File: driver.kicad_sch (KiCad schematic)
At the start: 39 parts, among them Q4 SIZ322DT, Q5 SIZ322DT, Q6 SIZ322DT, U4 TMC6200

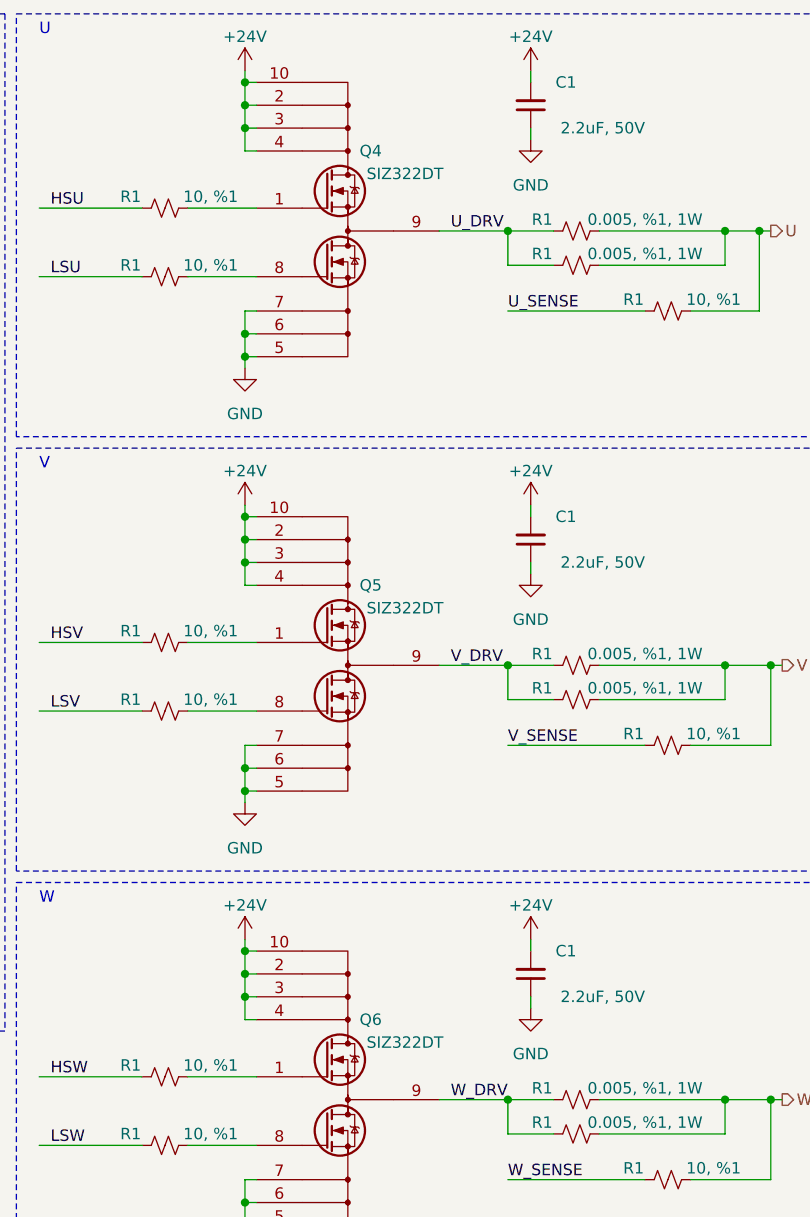
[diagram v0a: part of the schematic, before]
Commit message: Change the mosfets to SIZ342ADT.
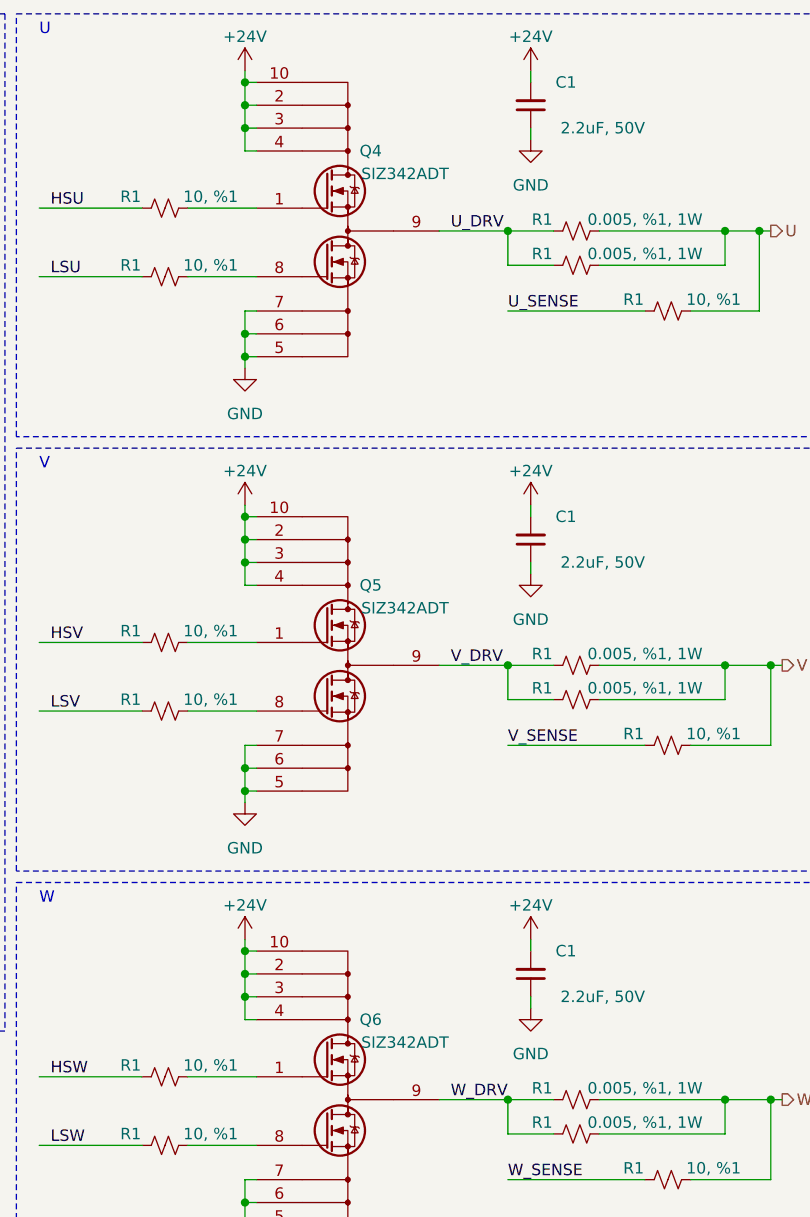
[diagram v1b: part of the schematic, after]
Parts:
- Q4, Q5, Q6: value SIZ322DT -> SIZ342ADT; MPN SIZ322DT-T1-GE3 -> SIZ342ADT-T1-GE3
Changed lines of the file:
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@@
       (effects (font (size 1.27 1.27)))
     )
-    (property "Value" "SIZ322DT" (at 226.06 129.54 0)
+    (property "Value" "SIZ342ADT" (at 226.06 129.54 0)
       (effects (font (size 1.27 1.27)))
     )
@@
       (effects (font (size 1.27 1.27)) (justify left top) hide)
     )
-    (property "MPN" "SIZ322DT-T1-GE3" (at 219.71 134.62 0)
+    (property "MPN" "SIZ342ADT-T1-GE3" (at 219.71 134.62 0)
       (effects (font (size 1.27 1.27)) hide)
     )
@@
       (effects (font (size 1.27 1.27)))
     )
-    (property "Value" "SIZ322DT" (at 226.06 33.02 0)
+    (property "Value" "SIZ342ADT" (at 226.06 33.02 0)
       (effects (font (size 1.27 1.27)))
     )
@@
       (effects (font (size 1.27 1.27)) (justify left top) hide)
     )
-    (property "MPN" "SIZ322DT-T1-GE3" (at 219.71 38.1 0)
+    (property "MPN" "SIZ342ADT-T1-GE3" (at 219.71 38.1 0)
       (effects (font (size 1.27 1.27)) hide)
     )
@@
       (effects (font (size 1.27 1.27)))
     )
-    (property "Value" "SIZ322DT" (at 226.06 81.28 0)
+    (property "Value" "SIZ342ADT" (at 226.06 81.28 0)
       (effects (font (size 1.27 1.27)))
     )
@@
       (effects (font (size 1.27 1.27)) (justify left top) hide)
     )
-    (property "MPN" "SIZ322DT-T1-GE3" (at 219.71 86.36 0)
-      (effects (font (size 1.27 1.27)) hide)
-    )
+    (property "MPN" "SIZ342ADT-T1-GE3" (at 219.71 86.36 0)
+      (effects (font (size 1.27 1.27)) hide)
+    )

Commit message: Small improvements.
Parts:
- C1: footprint Capacitor_SMD:C_1206_3216Metric -> Capacitor_SMD:C_0805_2012Metric; MPN CL31B225KBHNNNE -> CC0805KKX7R9BB225
- C22: value 100nF, 100V -> 100nF, 50V; footprint Capacitor_SMD:C_0603_1608Metric -> Capacitor_SMD:C_0402_1005Metric; MPN CL10B104KC8NNNC -> GRM155R71H104KE14J
- C22: MPN UMK212BB7225KG-T -> CC0805KKX7R9BB225
- C22: MPN CL05B104KB54PNC -> GRM155R71H104KE14J
- C22: value 22nF, 100V -> 22nF, 50V; footprint Capacitor_SMD:C_0603_1608Metric -> Capacitor_SMD:C_0402_1005Metric; MPN C0603C223K1RAC7867 -> GRM155R71H223KA12J
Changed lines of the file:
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@@
       (effects (font (size 1.27 1.27)) (justify left))
     )
-    (property "Value" "100nF, 100V" (at 59.69 41.91 0)
-      (effects (font (size 1.27 1.27)) (justify left))
-    )
-    (property "Footprint" "Capacitor_SMD:C_0603_1608Metric" (at 60.96 39.37 0)
+    (property "Value" "100nF, 50V" (at 59.69 41.91 0)
+      (effects (font (size 1.27 1.27)) (justify left))
+    )
+    (property "Footprint" "Capacitor_SMD:C_0402_1005Metric" (at 60.96 39.37 0)
       (effects (font (size 1.27 1.27)) hide)
     )
@@
       (effects (font (size 1.27 1.27)) hide)
     )
-    (property "MPN" "CL10B104KC8NNNC" (at 60.96 39.37 0)
+    (property "MPN" "GRM155R71H104KE14J" (at 60.96 39.37 0)
       (effects (font (size 1.27 1.27)) hide)
     )
@@
       (effects (font (size 1.27 1.27)) hide)
     )
-    (property "MPN" "UMK212BB7225KG-T" (at 33.02 55.88 0)
+    (property "MPN" "CC0805KKX7R9BB225" (at 33.02 55.88 0)
       (effects (font (size 1.27 1.27)) hide)
     )
@@
       (effects (font (size 1.27 1.27)) hide)
     )
-    (property "MPN" "CL05B104KB54PNC" (at 67.31 113.03 0)
+    (property "MPN" "GRM155R71H104KE14J" (at 67.31 113.03 0)
       (effects (font (size 1.27 1.27)) hide)
     )
@@
       (effects (font (size 1.27 1.27)) (justify left))
     )
-    (property "Value" "100nF, 100V" (at 111.76 30.48 90)
-      (effects (font (size 1.27 1.27)) (justify left))
-    )
-    (property "Footprint" "Capacitor_SMD:C_0603_1608Metric" (at 106.68 27.94 0)
+    (property "Value" "100nF, 50V" (at 111.76 30.48 90)
+      (effects (font (size 1.27 1.27)) (justify left))
+    )
+    (property "Footprint" "Capacitor_SMD:C_0402_1005Metric" (at 106.68 27.94 0)
       (effects (font (size 1.27 1.27)) hide)
     )
@@
       (effects (font (size 1.27 1.27)) hide)
     )
-    (property "MPN" "CL10B104KC8NNNC" (at 106.68 27.94 0)
+    (property "MPN" "GRM155R71H104KE14J" (at 106.68 27.94 0)
       (effects (font (size 1.27 1.27)) hide)
     )
@@
       (effects (font (size 1.27 1.27)) hide)
     )
-    (property "MPN" "CL05B104KB54PNC" (at 166.37 109.22 0)
+    (property "MPN" "GRM155R71H104KE14J" (at 166.37 109.22 0)
       (effects (font (size 1.27 1.27)) hide)
     )
@@
       (effects (font (size 1.27 1.27)) (justify left))
     )
-    (property "Value" "100nF, 100V" (at 130.81 33.02 0)
-      (effects (font (size 1.27 1.27)) (justify left))
-    )
-    (property "Footprint" "Capacitor_SMD:C_0603_1608Metric" (at 118.11 30.48 0)
+    (property "Value" "100nF, 50V" (at 130.81 33.02 0)
+      (effects (font (size 1.27 1.27)) (justify left))
+    )
+    (property "Footprint" "Capacitor_SMD:C_0402_1005Metric" (at 118.11 30.48 0)
       (effects (font (size 1.27 1.27)) hide)
     )
@@
       (effects (font (size 1.27 1.27)) hide)
     )
-    (property "MPN" "CL10B104KC8NNNC" (at 118.11 30.48 0)
+    (property "MPN" "GRM155R71H104KE14J" (at 118.11 30.48 0)
       (effects (font (size 1.27 1.27)) hide)
     )
@@
       (effects (font (size 1.27 1.27)) (justify left))
     )
-    (property "Value" "22nF, 100V" (at 97.79 30.48 90)
-      (effects (font (size 1.27 1.27)) (justify left))
-    )
-    (property "Footprint" "Capacitor_SMD:C_0603_1608Metric" (at 92.71 27.94 0)
+    (property "Value" "22nF, 50V" (at 97.79 30.48 90)
+      (effects (font (size 1.27 1.27)) (justify left))
+    )
+    (property "Footprint" "Capacitor_SMD:C_0402_1005Metric" (at 92.71 27.94 0)
       (effects (font (size 1.27 1.27)) hide)
     )
@@
       (effects (font (size 1.27 1.27)) hide)
     )
-    (property "MPN" "C0603C223K1RAC7867" (at 92.71 27.94 90)
+    (property "MPN" "GRM155R71H223KA12J" (at 92.71 27.94 90)
       (effects (font (size 1.27 1.27)) hide)
     )
@@
       (effects (font (size 1.27 1.27)) hide)
     )
-    (property "MPN" "UMK212BB7225KG-T" (at 46.99 55.88 0)
+    (property "MPN" "CC0805KKX7R9BB225" (at 46.99 55.88 0)
       (effects (font (size 1.27 1.27)) hide)
     )
@@
       (effects (font (size 1.27 1.27)) (justify left))
     )
-    (property "Footprint" "Capacitor_SMD:C_1206_3216Metric" (at 240.03 25.4 0)
+    (property "Footprint" "Capacitor_SMD:C_0805_2012Metric" (at 240.03 25.4 0)
       (effects (font (size 1.27 1.27)) hide)
     )
@@
       (effects (font (size 1.27 1.27)) hide)
     )
-    (property "MPN" "CL31B225KBHNNNE" (at 240.03 25.4 0)
+    (property "MPN" "CC0805KKX7R9BB225" (at 240.03 25.4 0)
       (effects (font (size 1.27 1.27)) hide)
     )
@@
       (effects (font (size 1.27 1.27)) (justify left))
     )
-    (property "Footprint" "Capacitor_SMD:C_1206_3216Metric" (at 240.03 73.66 0)
+    (property "Footprint" "Capacitor_SMD:C_0805_2012Metric" (at 240.03 73.66 0)
       (effects (font (size 1.27 1.27)) hide)
     )
@@
       (effects (font (size 1.27 1.27)) hide)
     )
-    (property "MPN" "CL31B225KBHNNNE" (at 240.03 73.66 0)
+    (property "MPN" "CC0805KKX7R9BB225" (at 240.03 73.66 0)
       (effects (font (size 1.27 1.27)) hide)
     )
@@
       (effects (font (size 1.27 1.27)) (justify left))
     )
-    (property "Footprint" "Capacitor_SMD:C_1206_3216Metric" (at 240.03 121.92 0)
+    (property "Footprint" "Capacitor_SMD:C_0805_2012Metric" (at 240.03 121.92 0)
       (effects (font (size 1.27 1.27)) hide)
     )
@@
       (effects (font (size 1.27 1.27)) hide)
     )
-    (property "MPN" "CL31B225KBHNNNE" (at 240.03 121.92 0)
-      (effects (font (size 1.27 1.27)) hide)
-    )
+    (property "MPN" "CC0805KKX7R9BB225" (at 240.03 121.92 0)
+      (effects (font (size 1.27 1.27)) hide)
+    )
